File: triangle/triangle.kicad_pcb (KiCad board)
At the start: 2 copper layers, 55.8 x 49.1 mm, 15 parts, among them J1 GND, J2 DIN, J3 5V, J4 GND, J5 DOUT, J6 5V, J7 GND, J8 DOUT, J9 5V

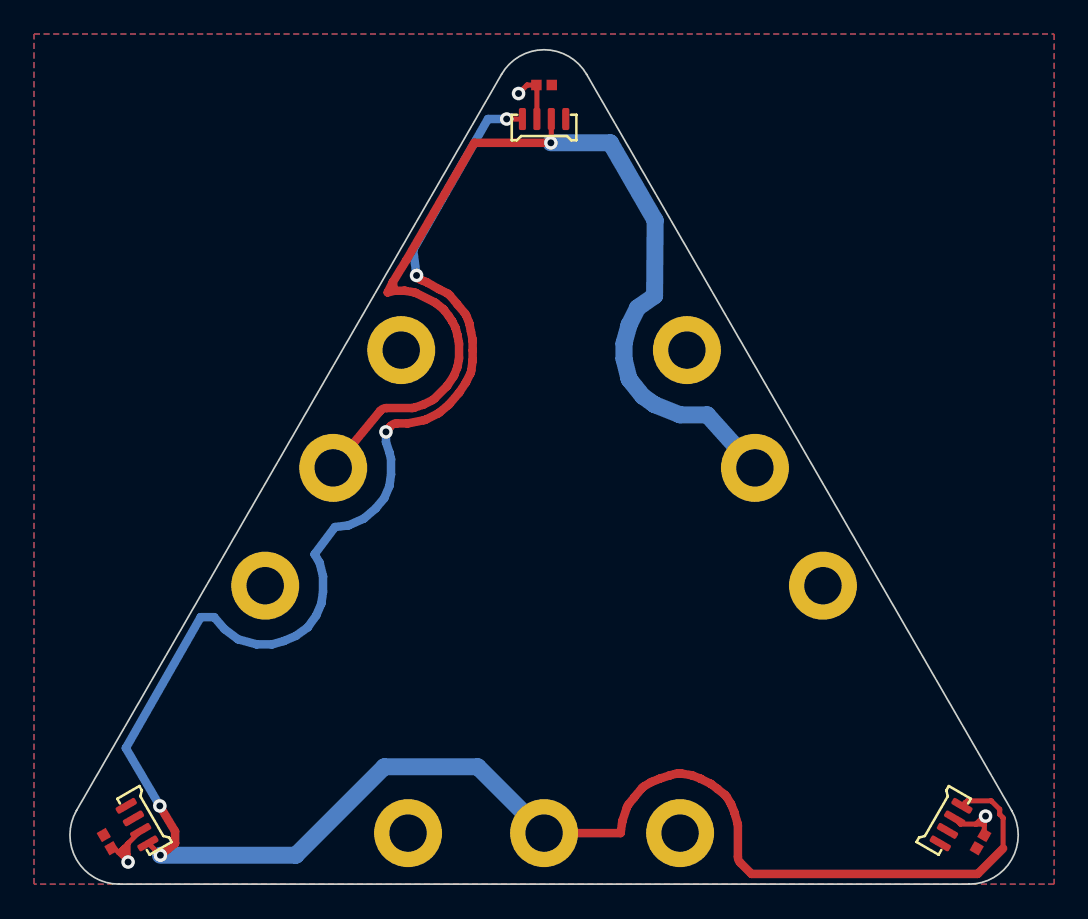
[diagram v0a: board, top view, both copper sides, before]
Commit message: Add tooling holes
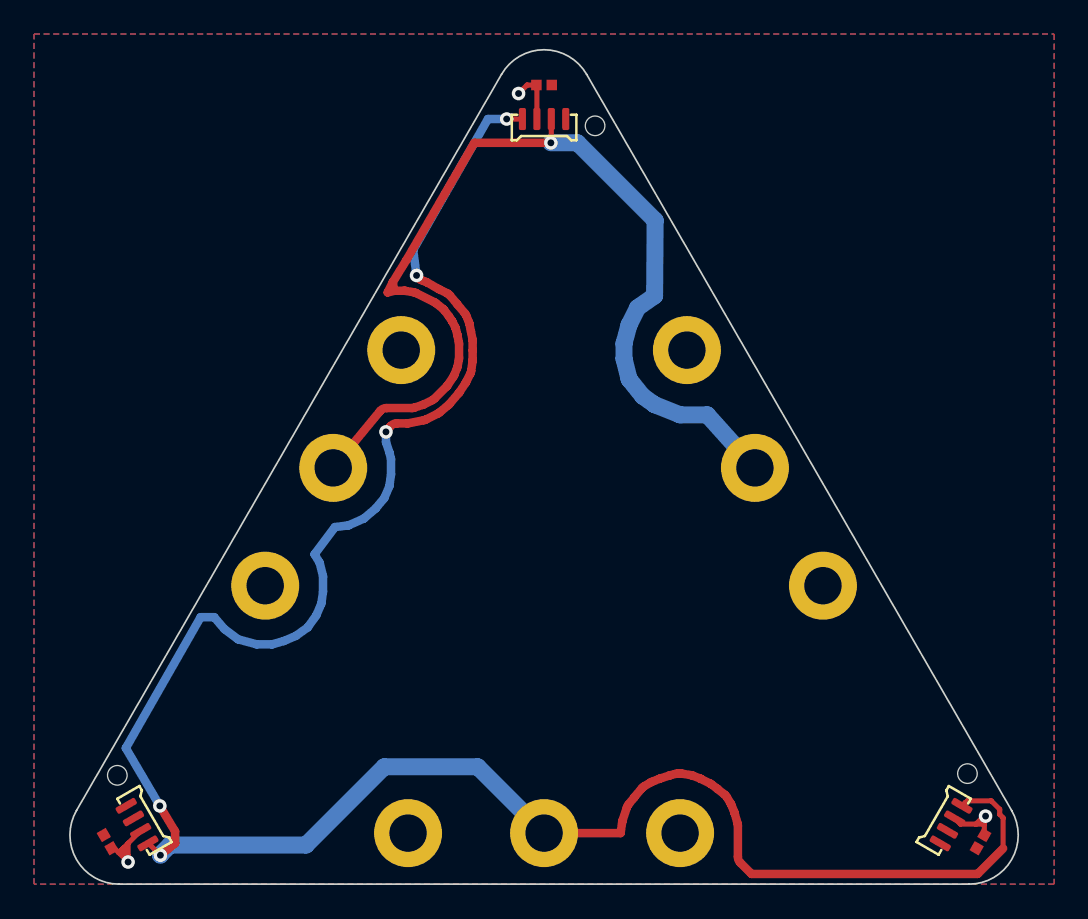
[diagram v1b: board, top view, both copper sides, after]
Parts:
- added X1: TOOLING, agg:M2.5_HOLE, F.Cu at (154.9, 133.5)
- added X2: TOOLING, agg:M2.5_HOLE, F.Cu at (133.0, 95.4)
- added X3: TOOLING, agg:M2.5_HOLE, F.Cu at (104.9, 133.6)
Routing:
- net /DOUT: track 62.2 -> 61.5 mm

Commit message: Update triangle board to put LED centroid at footprint origin
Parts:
- moved LED1 0.70 mm to (153.3, 136.2)
- moved LED2 0.70 mm to (106.7, 136.2)
- moved LED3 0.70 mm to (130.0, 95.7)
